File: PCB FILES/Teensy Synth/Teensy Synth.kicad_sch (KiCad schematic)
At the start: 97 parts, among them J1 Conn_01x05, SW1 SW_Push, SW10 SW_Push, SW11 SW_Push, SW12 SW_Push, SW13 SW_Push, SW14 SW_Push, SW15 SW_Push, SW16 SW_Push, SW17 SW_Push, SW18 SW_Push, SW19 SW_Push, SW2 SW_Push, SW20 SW_Push, SW21 SW_Push, SW22 SW_Push, SW23 SW_Push, SW24 SW_Push, SW25 SW_Push, SW26 SW_Push, SW27 SW_Push, SW28 SW_Push, SW29 SW_Push, SW3 SW_Push, SW30 SW_Push, SW31 SW_Push, SW32 SW_Push, SW33 SW_Push, SW34 SW_Push, SW35 SW_Push, SW36 SW_Push, SW37 SW_Push, SW38 SW_Push, SW39 SW_Push, SW4 SW_Push, SW40 SW_Push, SW41 SW_Push, SW42 SW_Push, SW43 SW_Push, SW44 SW_Push, SW45 SW_Push, SW46 SW_Push, SW47 SW_Push, SW5 SW_Push, SW6 SW_Push, SW7 SW_Push, SW8 SW_Push, SW9 SW_Push, U1 Teensy4.1, U2 RP2040

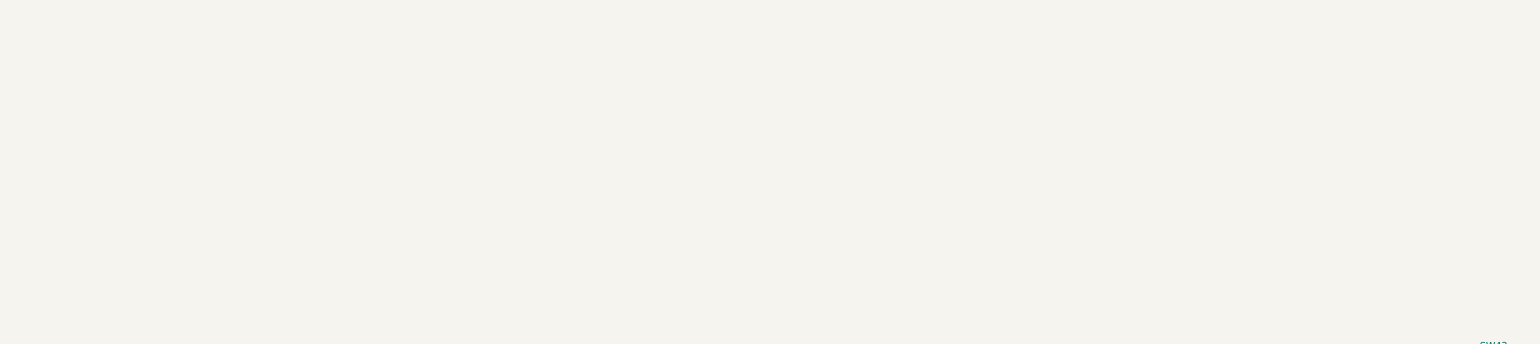
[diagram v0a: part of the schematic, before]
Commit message: Addded encoders (4+1)
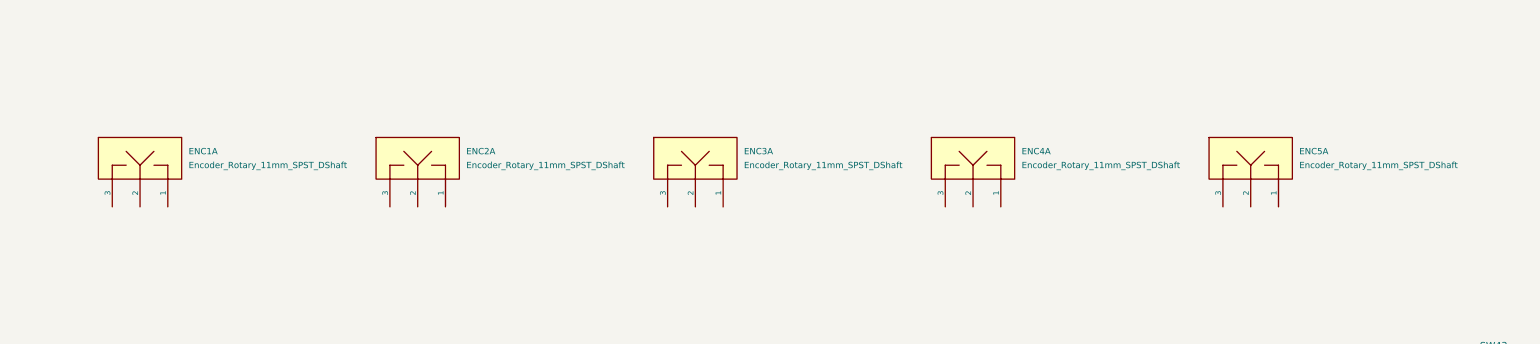
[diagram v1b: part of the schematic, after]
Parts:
- added ENC1, ENC2, ENC3, ENC4, ENC5: Encoder_Rotary_11mm_SPST_DShaft, 4ms_Encoder:ENC_SPST_12mm, symbol PCM_4ms_Switch:Encoder_Rotary_11mm_SPST_DShaft
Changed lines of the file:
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@@
+    )
+  )
+  (symbol (lib_id "PCM_4ms_Switch:Encoder_Rotary_11mm_SPST_DShaft") (at 341.63 220.98 0) (unit 1)
+    (in_bom yes) (on_board yes) (dnp no) (fields_autoplaced)
+    (property "Reference" "ENC4" (at 350.52 215.9 0)
+      (effects (font (size 1.143 1.143)) (justify left))
+    )
+    (property "Value" "Encoder_Rotary_11mm_SPST_DShaft" (at 350.52 218.44 0)
+      (effects (font (size 1.143 1.143)) (justify left))
+    )
+    (property "Footprint" "4ms_Encoder:ENC_SPST_12mm" (at 342.265 208.28 0)
+      (effects (font (size 0.508 0.508)) hide)
+    )
+    (property "Datasheet" "" (at 332.74 227.33 0)
+      (effects (font (size 1.524 1.524)) hide)
+    )
+    (property "Manufacturer" "Alpha Taiwan" (at 341.63 233.68 0)
+      (effects (font (size 1.27 1.27)) hide)
+    )
+    (property "Part Number" "RE111F-41B3N-20F-20P-N" (at 341.63 236.22 0)
+      (effects (font (size 1.27 1.27)) hide)
+    )
+    (property "Specifications" "Rotary Encoder 11mm with SPST, No Detent, 20mm D-shaft" (at 344.17 231.14 0)
+      (effects (font (size 1.27 1.27)) hide)
+    )
+    (property "Manufacturer 2" "Bourns" (at 341.63 238.76 0)
+      (effects (font (size 1.27 1.27)) hide)
+    )
+    (property "Part Number 2" "PEC11L-4020F-S0020" (at 342.9 241.3 0)
+      (effects (font (size 1.27 1.27)) hide)
+    )
+    (pin "1")
+    (pin "2")
+    (pin "3")
+    (pin "SW1")
+    (pin "SW2")
+    (instances
+      (project "Teensy Synth"
+        (path "/c9e64777-b068-4bbd-bb2c-e1f5e825559e"
+          (reference "ENC4") (unit 1)
+        )
+      )
     )
   )
@@
     )
   )
+  (symbol (lib_id "PCM_4ms_Switch:Encoder_Rotary_11mm_SPST_DShaft") (at 290.83 220.98 0) (unit 1)
+    (in_bom yes) (on_board yes) (dnp no) (fields_autoplaced)
+    (property "Reference" "ENC3" (at 299.72 215.9 0)
+      (effects (font (size 1.143 1.143)) (justify left))
+    )
+    (property "Value" "Encoder_Rotary_11mm_SPST_DShaft" (at 299.72 218.44 0)
+      (effects (font (size 1.143 1.143)) (justify left))
+    )
+    (property "Footprint" "4ms_Encoder:ENC_SPST_12mm" (at 291.465 208.28 0)
+      (effects (font (size 0.508 0.508)) hide)
+    )
+    (property "Datasheet" "" (at 281.94 227.33 0)
+      (effects (font (size 1.524 1.524)) hide)
+    )
+    (property "Manufacturer" "Alpha Taiwan" (at 290.83 233.68 0)
+      (effects (font (size 1.27 1.27)) hide)
+    )
+    (property "Part Number" "RE111F-41B3N-20F-20P-N" (at 290.83 236.22 0)
+      (effects (font (size 1.27 1.27)) hide)
+    )
+    (property "Specifications" "Rotary Encoder 11mm with SPST, No Detent, 20mm D-shaft" (at 293.37 231.14 0)
+      (effects (font (size 1.27 1.27)) hide)
+    )
+    (property "Manufacturer 2" "Bourns" (at 290.83 238.76 0)
+      (effects (font (size 1.27 1.27)) hide)
+    )
+    (property "Part Number 2" "PEC11L-4020F-S0020" (at 292.1 241.3 0)
+      (effects (font (size 1.27 1.27)) hide)
+    )
+    (pin "1")
+    (pin "2")
+    (pin "3")
+    (pin "SW1")
+    (pin "SW2")
+    (instances
+      (project "Teensy Synth"
+        (path "/c9e64777-b068-4bbd-bb2c-e1f5e825559e"
+          (reference "ENC3") (unit 1)
+        )
+      )
+    )
+  )
   (symbol (lib_id "Switch:SW_Push") (at 309.88 297.18 0) (unit 1)
     (in_bom yes) (on_board yes) (dnp no) (fields_autoplaced)
@@
     )
   )
+  (symbol (lib_id "PCM_4ms_Switch:Encoder_Rotary_11mm_SPST_DShaft") (at 240.03 220.98 0) (unit 1)
+    (in_bom yes) (on_board yes) (dnp no) (fields_autoplaced)
+    (property "Reference" "ENC2" (at 248.92 215.9 0)
+      (effects (font (size 1.143 1.143)) (justify left))
+    )
+    (property "Value" "Encoder_Rotary_11mm_SPST_DShaft" (at 248.92 218.44 0)
+      (effects (font (size 1.143 1.143)) (justify left))
+    )
+    (property "Footprint" "4ms_Encoder:ENC_SPST_12mm" (at 240.665 208.28 0)
+      (effects (font (size 0.508 0.508)) hide)
+    )
+    (property "Datasheet" "" (at 231.14 227.33 0)
+      (effects (font (size 1.524 1.524)) hide)
+    )
+    (property "Manufacturer" "Alpha Taiwan" (at 240.03 233.68 0)
+      (effects (font (size 1.27 1.27)) hide)
+    )
+    (property "Part Number" "RE111F-41B3N-20F-20P-N" (at 240.03 236.22 0)
+      (effects (font (size 1.27 1.27)) hide)
+    )
+    (property "Specifications" "Rotary Encoder 11mm with SPST, No Detent, 20mm D-shaft" (at 242.57 231.14 0)
+      (effects (font (size 1.27 1.27)) hide)
+    )
+    (property "Manufacturer 2" "Bourns" (at 240.03 238.76 0)
+      (effects (font (size 1.27 1.27)) hide)
+    )
+    (property "Part Number 2" "PEC11L-4020F-S0020" (at 241.3 241.3 0)
+      (effects (font (size 1.27 1.27)) hide)
+    )
+    (pin "1")
+    (pin "2")
+    (pin "3")
+    (pin "SW1")
+    (pin "SW2")
+    (instances
+      (project "Teensy Synth"
+        (path "/c9e64777-b068-4bbd-bb2c-e1f5e825559e"
+          (reference "ENC2") (unit 1)
+        )
+      )
+    )
+  )
   (symbol (lib_id "Switch:SW_Push") (at 284.48 284.48 0) (unit 1)
     (in_bom yes) (on_board yes) (dnp no) (fields_autoplaced)
@@
     )
   )
+  (symbol (lib_id "PCM_4ms_Switch:Encoder_Rotary_11mm_SPST_DShaft") (at 392.43 220.98 0) (unit 1)
+    (in_bom yes) (on_board yes) (dnp no) (fields_autoplaced)
+    (property "Reference" "ENC5" (at 401.32 215.9 0)
+      (effects (font (size 1.143 1.143)) (justify left))
+    )
+    (property "Value" "Encoder_Rotary_11mm_SPST_DShaft" (at 401.32 218.44 0)
+      (effects (font (size 1.143 1.143)) (justify left))
+    )
+    (property "Footprint" "4ms_Encoder:ENC_SPST_12mm" (at 393.065 208.28 0)
+      (effects (font (size 0.508 0.508)) hide)
+    )
+    (property "Datasheet" "" (at 383.54 227.33 0)
+      (effects (font (size 1.524 1.524)) hide)
+    )
+    (property "Manufacturer" "Alpha Taiwan" (at 392.43 233.68 0)
+      (effects (font (size 1.27 1.27)) hide)
+    )
+    (property "Part Number" "RE111F-41B3N-20F-20P-N" (at 392.43 236.22 0)
+      (effects (font (size 1.27 1.27)) hide)
+    )
+    (property "Specifications" "Rotary Encoder 11mm with SPST, No Detent, 20mm D-shaft" (at 394.97 231.14 0)
+      (effects (font (size 1.27 1.27)) hide)
+    )
+    (property "Manufacturer 2" "Bourns" (at 392.43 238.76 0)
+      (effects (font (size 1.27 1.27)) hide)
+    )
+    (property "Part Number 2" "PEC11L-4020F-S0020" (at 393.7 241.3 0)
+      (effects (font (size 1.27 1.27)) hide)
+    )
+    (pin "1")
+    (pin "2")
+    (pin "3")
+    (pin "SW1")
+    (pin "SW2")
+    (instances
+      (project "Teensy Synth"
+        (path "/c9e64777-b068-4bbd-bb2c-e1f5e825559e"
+          (reference "ENC5") (unit 1)
+        )
+      )
+    )
+  )
   (symbol (lib_id "Device:D") (at 279.4 326.39 90) (unit 1)
     (in_bom yes) (on_board yes) (dnp no) (fields_autoplaced)
@@
         )
       )
+    )
+  )
+  (symbol (lib_id "PCM_4ms_Switch:Encoder_Rotary_11mm_SPST_DShaft") (at 189.23 220.98 0) (unit 1)
+    (in_bom yes) (on_board yes) (dnp no) (fields_autoplaced)
+    (property "Reference" "ENC1" (at 198.12 215.9 0)
+      (effects (font (size 1.143 1.143)) (justify left))
+    )
+    (property "Value" "Encoder_Rotary_11mm_SPST_DShaft" (at 198.12 218.44 0)
+      (effects (font (size 1.143 1.143)) (justify left))
+    )
+    (property "Footprint" "4ms_Encoder:ENC_SPST_12mm" (at 189.865 208.28 0)
+      (effects (font (size 0.508 0.508)) hide)
+    )
+    (property "Datasheet" "" (at 180.34 227.33 0)
+      (effects (font (size 1.524 1.524)) hide)
+    )
+    (property "Manufacturer" "Alpha Taiwan" (at 189.23 233.68 0)
+      (effects (font (size 1.27 1.27)) hide)
+    )
+    (property "Part Number" "RE111F-41B3N-20F-20P-N" (at 189.23 236.22 0)
+      (effects (font (size 1.27 1.27)) hide)
+    )
+    (property "Specifications" "Rotary Encoder 11mm with SPST, No Detent, 20mm D-shaft" (at 191.77 231.14 0)
+      (effects (font (size 1.27 1.27)) hide)
+    )
+    (property "Manufacturer 2" "Bourns" (at 189.23 238.76 0)
+      (effects (font (size 1.27 1.27)) hide)
+    )
+    (property "Part Number 2" "PEC11L-4020F-S0020" (at 190.5 241.3 0)
+      (effects (font (size 1.27 1.27)) hide)
+    )
+    (pin "1")
+    (pin "2")
+    (pin "3")
+    (pin "SW1")
+    (pin "SW2")
+    (instances
+      (project "Teensy Synth"
+        (path "/c9e64777-b068-4bbd-bb2c-e1f5e825559e"
+          (reference "ENC1") (unit 1)
+        )
+      )

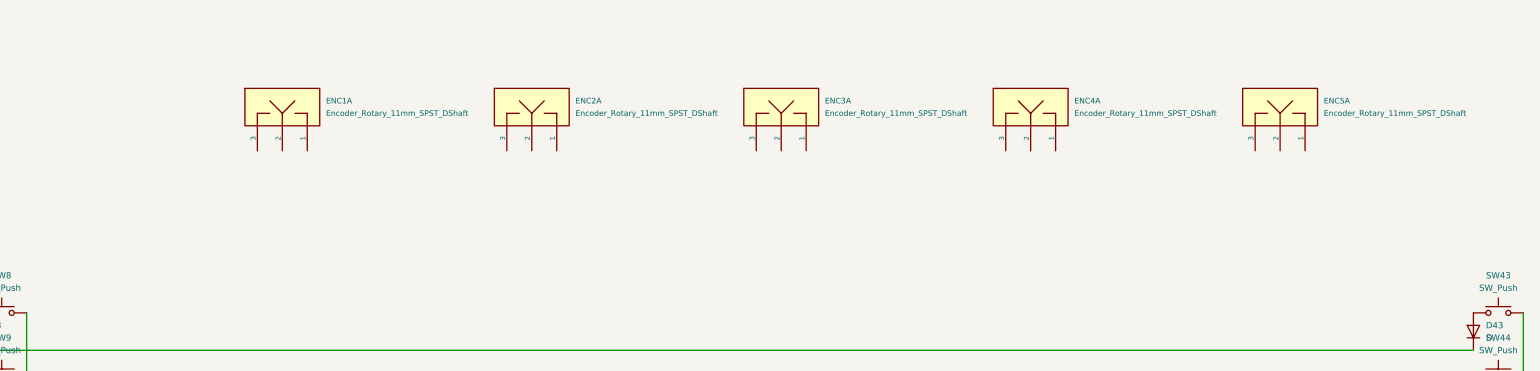
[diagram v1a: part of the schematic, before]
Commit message: Fixed and Labeled Encoders
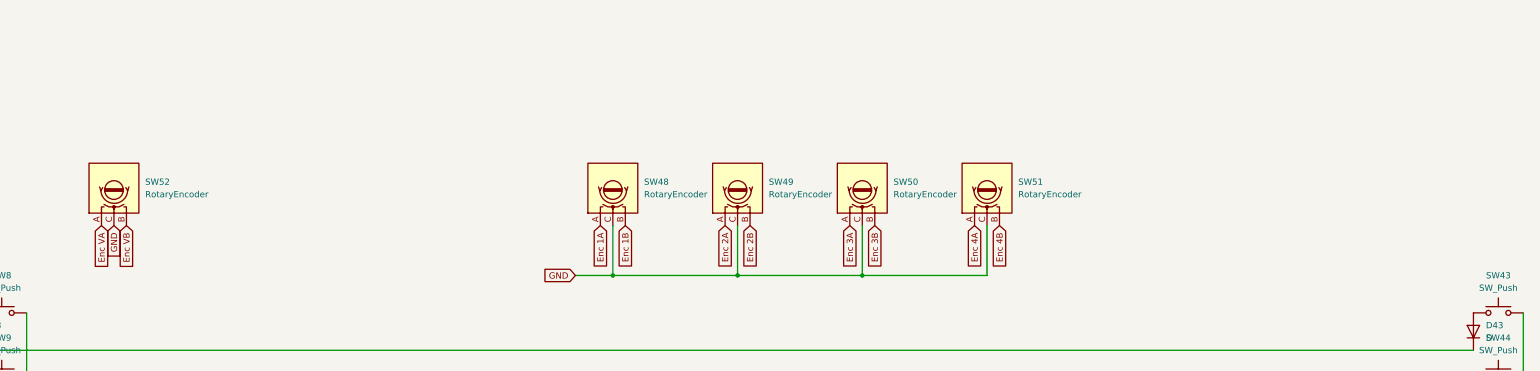
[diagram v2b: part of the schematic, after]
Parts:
- removed ENC1, ENC2, ENC3, ENC4, ENC5: Encoder_Rotary_11mm_SPST_DShaft, 4ms_Encoder:ENC_SPST_12mm, symbol PCM_4ms_Switch:Encoder_Rotary_11mm_SPST_DShaft
- added SW48, SW49, SW50, SW51, SW52: RotaryEncoder, symbol Device:RotaryEncoder
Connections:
- net GND: now also SW48.C, SW49.C, SW50.C, SW51.C, SW52.C
- new net Enc 1A: SW48.A
- new net Enc 1B: SW48.B
- new net Enc 2A: SW49.A
- new net Enc 2B: SW49.B
- new net Enc 3A: SW50.A
- new net Enc 3B: SW50.B
- new net Enc 4A: SW51.A
- new net Enc 4B: SW51.B
- new net Enc VA: SW52.A
- new net Enc VB: SW52.B
